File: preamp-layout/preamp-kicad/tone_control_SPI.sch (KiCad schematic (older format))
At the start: 54 parts

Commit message: Added preliminary gain stage
Gain stage added with choice of 6db or 12db gain. Cleaned up Gain stage IO pins on preamp sheet. Broke out volume ctrl to its own board, updated accordingly. Minor routing changes on preamp sheet.
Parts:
- removed C? (x11): C, symbol Device:C
- removed D?: LED, symbol Device:LED
- removed J?: Conn_01x03_Female, symbol Connector:Conn_01x03_Female
- removed J?: Conn_01x03_Male, symbol Connector:Conn_01x03_Male
- removed R? (x12): 10K, symbol Device:R
- removed U? (x4): TL072, symbol Amplifier_Operational:TL072
- added C? (x11): C, symbol Device:C
- added D?: LED, symbol Device:LED
- added J?: Conn_01x03_Female, symbol Connector:Conn_01x03_Female
- added J?: Conn_01x03_Male, symbol Connector:Conn_01x03_Male
- added R? (x12): 10K, symbol Device:R
- added U? (x4): TL072, symbol Amplifier_Operational:TL072
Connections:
- net +15V: now also J?.1 (Pin_1), J?.1 (Pin_1), U?.8 (V+), U?.8 (V+)
- net -15V: now also J?.2 (Pin_2), J?.2 (Pin_2), U?.4 (V-), U?.4 (V-)
- net GNDA: now also D?.2 (A), J?.3 (Pin_3), J?.3 (Pin_3), R?.2, U?.5 (+)
- net HF_L_A: now also R?.1
- net HF_L_B: now also R?.2
- net HF_L_W: now also C?.2
- net IN_R: now also C?.2
- net LF_L_A: now also R?.1
- net LF_L_B: now also R?.2
- net LF_L_W: now also R?.2
- net LF_R_A: now also C?.2, R?.1
- net LF_R_B: now also C?.1, R?.2
- net LMF_L_A: now also C?.2
- net LMF_L_B: now also C?.1
- net LMF_L_W: now also C?.2
- net LMF_R_A: now also C?.2
- net LMF_R_B: now also C?.1
- net OUT_L: now also R?.1, R?.1, R?.1
- net OUT_R: now also R?.1, R?.1, U?.7
- net UMF_L_A: now also C?.2, R?.1
- net UMF_L_B: now also C?.1, R?.2
- net UMF_R_A: now also C?.2, R?.1
- net UMF_R_B: now also C?.1, R?.2
- net UMF_R_W: now also C?.2
- net at R?.2, R?.2: now also C?.2, R?.2, R?.2
- net at C?.1, C?.1, R?.1: now also C?.1, U?.6 (-)
- net at R?.2: now also C?.2, R?.2, R?.2, R?.2
- net at C?.1, U?.6 (-): now also C?.1, C?.1, R?.1
- net at U?.1, U?.2 (-): now also C?.1
- net at R?.2: now also D?.1 (K)
- new net: C?.1, U?.1, U?.2 (-)
- new net: C?.1, R?.1, U?.3 (+)

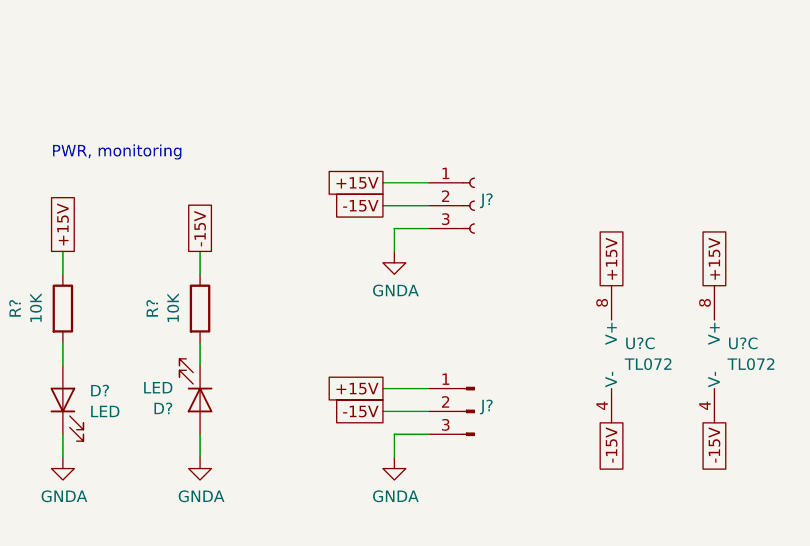
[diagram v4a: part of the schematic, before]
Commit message: Created component library, changed connector pinouts
Project library was created for this project to house custom parts, starting with Omron relay. 15V supply conn output changed so that pin 1 remains +15V, but pin 2 is now common and pin 3 is now -15V. SImilarly, 3 pin audio conn changed so that pin 2 is common and pin 3 is Right channel.

Implemented new schematic symbol for relays, general sheet cleanup. Removed MISO from IO selector board.
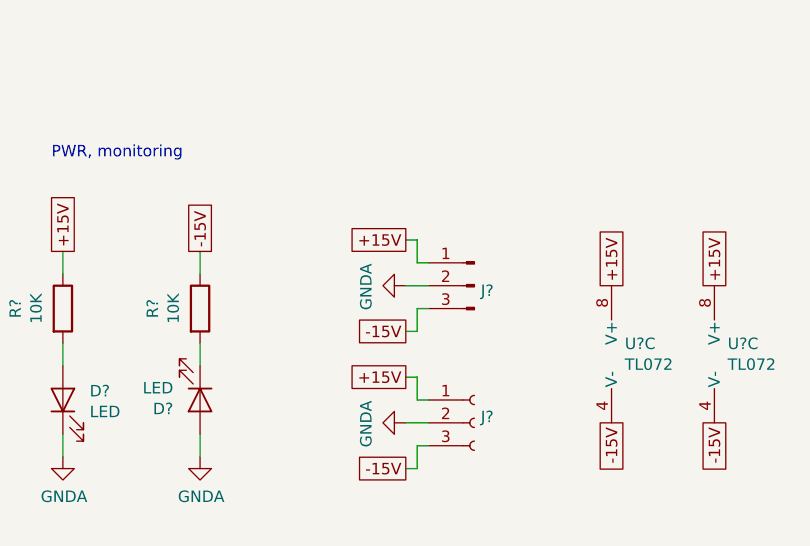
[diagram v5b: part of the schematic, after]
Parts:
- removed J?: Conn_01x03_Female, symbol Connector:Conn_01x03_Female
- removed J?: Conn_01x03_Male, symbol Connector:Conn_01x03_Male
- added J?: Conn_01x03_Male, symbol Connector:Conn_01x03_Male
- added J?: Conn_01x03_Female, symbol Connector:Conn_01x03_Female
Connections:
- net +15V: now also J?.1 (Pin_1), J?.1 (Pin_1)
- net -15V: now also J?.3 (Pin_3), J?.3 (Pin_3)
- net GNDA: now also J?.2 (Pin_2), J?.2 (Pin_2)
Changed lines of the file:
@@
-	1    0    0    -1
-$EndComp
-Text GLabel 4900 6200 0    50   UnSpc ~ 0
-+15V
-Text GLabel 4900 6300 0    50   UnSpc ~ 0
--15V
-$Comp
-L power:GNDA #PWR?
-U 1 1 60108088
-P 4950 6500
-AR Path="/5E2D8DA2/60108088" Ref="#PWR?"  Part="1"
-AR Path="/61DC5D9D/60108088" Ref="#PWR?"  Part="1"
-AR Path="/5F2E428C/60108088" Ref="#PWR?"  Part="1"
-F 0 "#PWR?" H 4950 6250 50  0001 C CNN
-F 1 "GNDA" H 4955 6327 50  0000 C CNN
-F 2 "" H 4950 6500 50  0001 C CNN
-F 3 "" H 4950 6500 50  0001 C CNN
-	1    4950 6500
-	1    0    0    -1
-$EndComp
-Wire Wire Line
-	4900 6200 5100 6200
-Wire Wire Line
-	4900 6300 5100 6300
-Wire Wire Line
-	5100 6400 4950 6400
-Wire Wire Line
-	4950 6400 4950 6500
-$Comp
-L Connector:Conn_01x03_Female J?
-U 1 1 60108089
-P 5300 6300
-AR Path="/5E2D8DA2/60108089" Ref="J?"  Part="1"
-AR Path="/61DC5D9D/60108089" Ref="J?"  Part="1"
-AR Path="/5F2E428C/60108089" Ref="J?"  Part="1"
-F 0 "J?" H 5328 6326 50  0000 L CNN
-F 1 "Conn_01x03_Female" H 5328 6235 50  0001 L CNN
-F 2 "" H 5300 6300 50  0001 C CNN
-F 3 "~" H 5300 6300 50  0001 C CNN
-	1    5300 6300
 	1    0    0    -1
 $EndComp
 Text Notes 3450 6100 0    50   ~ 0
 PWR, monitoring
-Text GLabel 4900 7100 0    50   UnSpc ~ 0
-+15V
-Text GLabel 4900 7200 0    50   UnSpc ~ 0
--15V
-$Comp
-L power:GNDA #PWR?
-U 1 1 6010808A
-P 4950 7400
-AR Path="/5E2D8DA2/6010808A" Ref="#PWR?"  Part="1"
-AR Path="/61DC5D9D/6010808A" Ref="#PWR?"  Part="1"
-AR Path="/5F2E428C/6010808A" Ref="#PWR?"  Part="1"
-F 0 "#PWR?" H 4950 7150 50  0001 C CNN
-F 1 "GNDA" H 4955 7227 50  0000 C CNN
-F 2 "" H 4950 7400 50  0001 C CNN
-F 3 "" H 4950 7400 50  0001 C CNN
-	1    4950 7400
-	1    0    0    -1
-$EndComp
-Wire Wire Line
-	4900 7100 5100 7100
-Wire Wire Line
-	4900 7200 5100 7200
-Wire Wire Line
-	5100 7300 4950 7300
-Wire Wire Line
-	4950 7300 4950 7400
-$Comp
-L Connector:Conn_01x03_Male J?
-U 1 1 6010808B
-P 5300 7200
-AR Path="/5E2D8DA2/6010808B" Ref="J?"  Part="1"
-AR Path="/61DC5D9D/6010808B" Ref="J?"  Part="1"
-AR Path="/5F2E428C/6010808B" Ref="J?"  Part="1"
-F 0 "J?" H 5272 7224 50  0000 R CNN
-F 1 "Conn_01x03_Male" H 5272 7133 50  0001 R CNN
-F 2 "" H 5300 7200 50  0001 C CNN
-F 3 "~" H 5300 7200 50  0001 C CNN
-	1    5300 7200
-	-1   0    0    -1
-$EndComp
 Text Notes 8350 5550 0    50   ~ 0
 Sends to amp
@@
 Text HLabel 900  1600 0    50   Input ~ 0
 CLK
+Text GLabel 5000 6450 0    50   UnSpc ~ 0
++15V
+Text GLabel 5000 6850 0    50   UnSpc ~ 0
+-15V
+$Comp
+L power:GNDA #PWR?
+U 1 1 647C3FA7
+P 5000 6650
+AR Path="/5E2D8DA2/647C3FA7" Ref="#PWR?"  Part="1"
+AR Path="/5E1A0CE1/647C3FA7" Ref="#PWR?"  Part="1"
+AR Path="/5E80BFEC/647C3FA7" Ref="#PWR?"  Part="1"
+AR Path="/5E27B612/647C3FA7" Ref="#PWR?"  Part="1"
+AR Path="/6009D432/647C3FA7" Ref="#PWR?"  Part="1"
+F 0 "#PWR?" H 5000 6400 50  0001 C CNN
+F 1 "GNDA" H 5005 6477 50  0000 C CNN
+F 2 "" H 5000 6650 50  0001 C CNN
+F 3 "" H 5000 6650 50  0001 C CNN
+	1    5000 6650
+	0    1    1    0
+$EndComp
+Wire Wire Line
+	5100 6650 5000 6650
+$Comp
+L Connector:Conn_01x03_Male J?
+U 1 1 647C3FAE
+P 5300 6650
+AR Path="/5E27B612/647C3FAE" Ref="J?"  Part="1"
+AR Path="/6009D432/647C3FAE" Ref="J?"  Part="1"
+F 0 "J?" H 5272 6628 50  0000 R CNN
+F 1 "Conn_01x03_Male" H 5272 6583 50  0001 R CNN
+F 2 "" H 5300 6650 50  0001 C CNN
+F 3 "~" H 5300 6650 50  0001 C CNN
+	1    5300 6650
+	-1   0    0    -1
+$EndComp
+$Comp
+L Connector:Conn_01x03_Female J?
+U 1 1 647C3FB4
+P 5300 7250
+AR Path="/5E607732/647C3FB4" Ref="J?"  Part="1"
+AR Path="/5E2D8DA2/647C3FB4" Ref="J?"  Part="1"
+AR Path="/6009D432/647C3FB4" Ref="J?"  Part="1"
+F 0 "J?" H 5328 7276 50  0000 L CNN
+F 1 "Conn_01x03_Female" H 5328 7185 50  0001 L CNN
+F 2 "" H 5300 7250 50  0001 C CNN
+F 3 "~" H 5300 7250 50  0001 C CNN
+	1    5300 7250
+	1    0    0    -1
+$EndComp
+Wire Wire Line
+	5100 6550 5050 6550
+Wire Wire Line
+	5050 6550 5050 6450
+Wire Wire Line
+	5050 6450 5000 6450
+Wire Wire Line
+	5100 6750 5050 6750
+Wire Wire Line
+	5050 6750 5050 6850
+Wire Wire Line
+	5050 6850 5000 6850
+Text GLabel 5000 7050 0    50   UnSpc ~ 0
++15V
+Text GLabel 5000 7450 0    50   UnSpc ~ 0
+-15V
+$Comp
+L power:GNDA #PWR?
+U 1 1 647C3FC2
+P 5000 7250
+AR Path="/5E2D8DA2/647C3FC2" Ref="#PWR?"  Part="1"
+AR Path="/5E1A0CE1/647C3FC2" Ref="#PWR?"  Part="1"
+AR Path="/5E80BFEC/647C3FC2" Ref="#PWR?"  Part="1"
+AR Path="/5E27B612/647C3FC2" Ref="#PWR?"  Part="1"
+AR Path="/6009D432/647C3FC2" Ref="#PWR?"  Part="1"
+F 0 "#PWR?" H 5000 7000 50  0001 C CNN
+F 1 "GNDA" H 5005 7077 50  0000 C CNN
+F 2 "" H 5000 7250 50  0001 C CNN
+F 3 "" H 5000 7250 50  0001 C CNN
+	1    5000 7250
+	0    1    1    0
+$EndComp
+Wire Wire Line
+	5100 7250 5000 7250
+Wire Wire Line
+	5100 7150 5050 7150
+Wire Wire Line
+	5050 7150 5050 7050
+Wire Wire Line
+	5050 7050 5000 7050
+Wire Wire Line
+	5100 7350 5050 7350
+Wire Wire Line
+	5050 7350 5050 7450
+Wire Wire Line
+	5050 7450 5000 7450
 $EndSCHEMATC

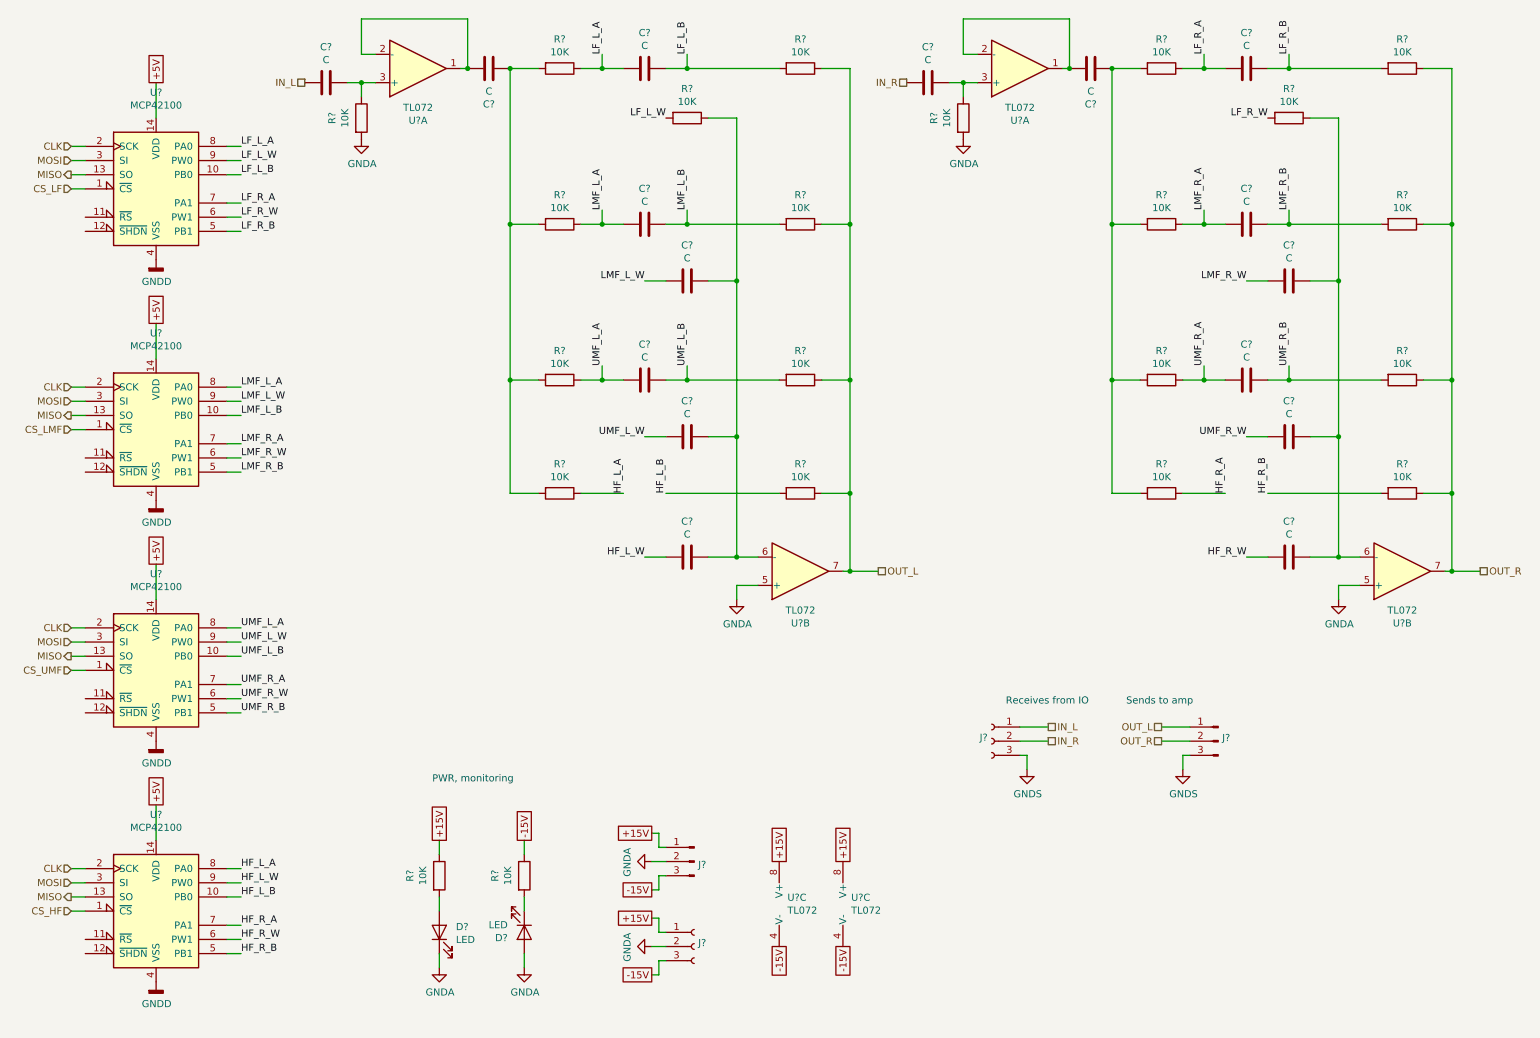
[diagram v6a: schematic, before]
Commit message: Grounds cleaned up, initial refdes numbering, error correction
GNDA, GNDS, GNDD, GND all combined to GND. No point in having separate grounds for this design.

Initial refdes numbering done using auto numbering feature. Error detection run and multple issues found which prompted Ground fix, as well as learning the disconnected pins require a 'no connection' flag to not throw an error.

Error correction also prompted the AC power connector symbol change to a plug to attempt to fix an error regarding 'driving' the circuit....more work to be done on error analysis.
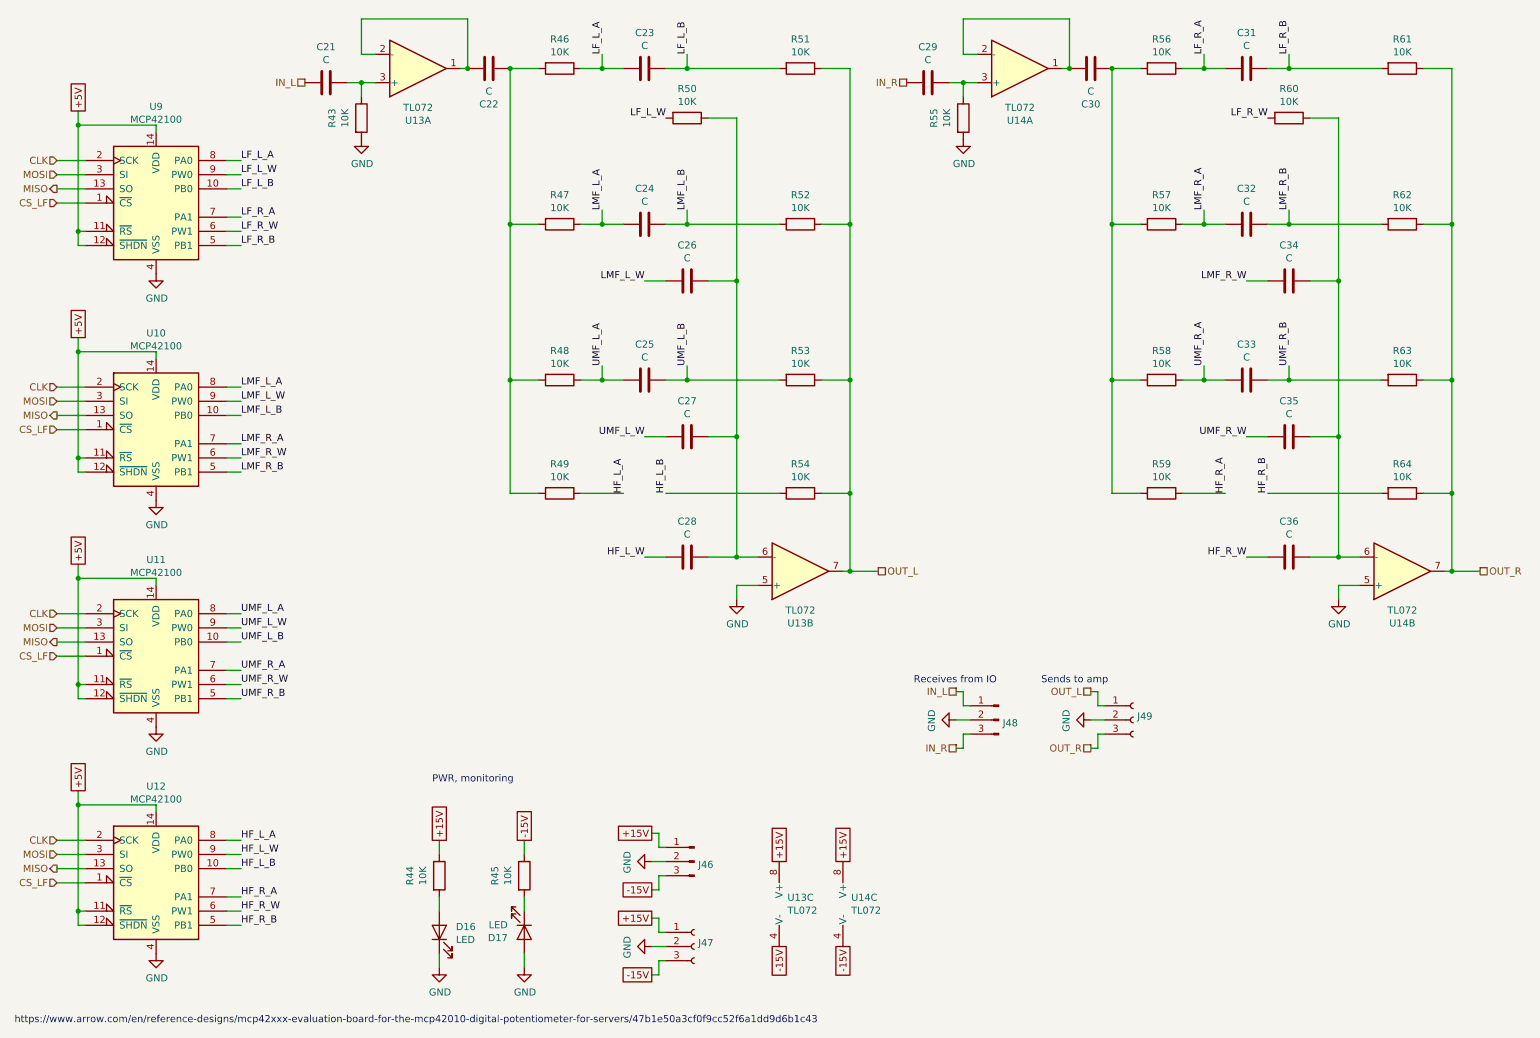
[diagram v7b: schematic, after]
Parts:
- removed J?: Conn_01x03_Female, symbol Connector:Conn_01x03_Female
- removed J?: Conn_01x03_Male, symbol Connector:Conn_01x03_Male
- removed U? (x3): MCP42100, symbol Potentiometer_Digital:MCP42100
- added J48: Conn_01x03_Male, symbol Connector:Conn_01x03_Male
- added J49: Conn_01x03_Female, symbol Connector:Conn_01x03_Female
- added U10, U11, U12: MCP42100, symbol Potentiometer_Digital:MCP42100
- gave numbers to parts that had none: 45
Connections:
- net GNDD is gone; now on net GND: U9.4 (VSS)
- net +5V: now also U9.11 (~RS), U9.12 (~SHDN), U10.11 (~RS), U10.12 (~SHDN), U10.14 (VDD), U11.11 (~RS), U11.12 (~SHDN), U11.14 (VDD), U12.11 (~RS), U12.12 (~SHDN), U12.14 (VDD)
- net CLK: now also U10.2 (SCK), U11.2 (SCK), U12.2 (SCK)
- net CS_LF: now also U10.1 (~CS), U11.1 (~CS), U12.1 (~CS)
- net HF_L_A: now also U12.8 (PA0)
- net HF_L_B: now also U12.10 (PB0)
- net HF_L_W: now also U12.9 (PW0)
- net HF_R_A: now also U12.7 (PA1)
- net HF_R_B: now also U12.5 (PB1)
- net HF_R_W: now also U12.6 (PW1)
- net IN_L: now also J48.1 (Pin_1)
- net IN_R: now also J48.3 (Pin_3)
- net LMF_L_A: now also U10.8 (PA0)
- net LMF_L_B: now also U10.10 (PB0)
- net LMF_L_W: now also U10.9 (PW0)
- net LMF_R_A: now also U10.7 (PA1)
- net LMF_R_B: now also U10.5 (PB1)
- net LMF_R_W: now also U10.6 (PW1)
- net MISO: now also U10.13 (SO), U11.13 (SO), U12.13 (SO)
- net MOSI: now also U10.3 (SI), U11.3 (SI), U12.3 (SI)
- net OUT_L: now also J49.1 (Pin_1)
- net OUT_R: now also J49.3 (Pin_3)
- net UMF_L_A: now also U11.8 (PA0)
- net UMF_L_B: now also U11.10 (PB0)
- net UMF_L_W: now also U11.9 (PW0)
- net UMF_R_A: now also U11.7 (PA1)
- net UMF_R_B: now also U11.5 (PB1)
- net UMF_R_W: now also U11.6 (PW1)
- net GNDA renamed GND
- net GND: now also J48.2 (Pin_2), J49.2 (Pin_2), U10.4 (VSS), U11.4 (VSS), U12.4 (VSS)
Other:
- note added: "https://www.arrow.com/en/reference-designs/mcp42xxx-evaluation-board-for-the-mcp42010-digital-potentiometer-for-servers/47b1e50a3cf0f9cc52f6a1dd9d6b1c43"
- moved on the sheet: U9
